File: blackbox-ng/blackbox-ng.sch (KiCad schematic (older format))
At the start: 19 parts

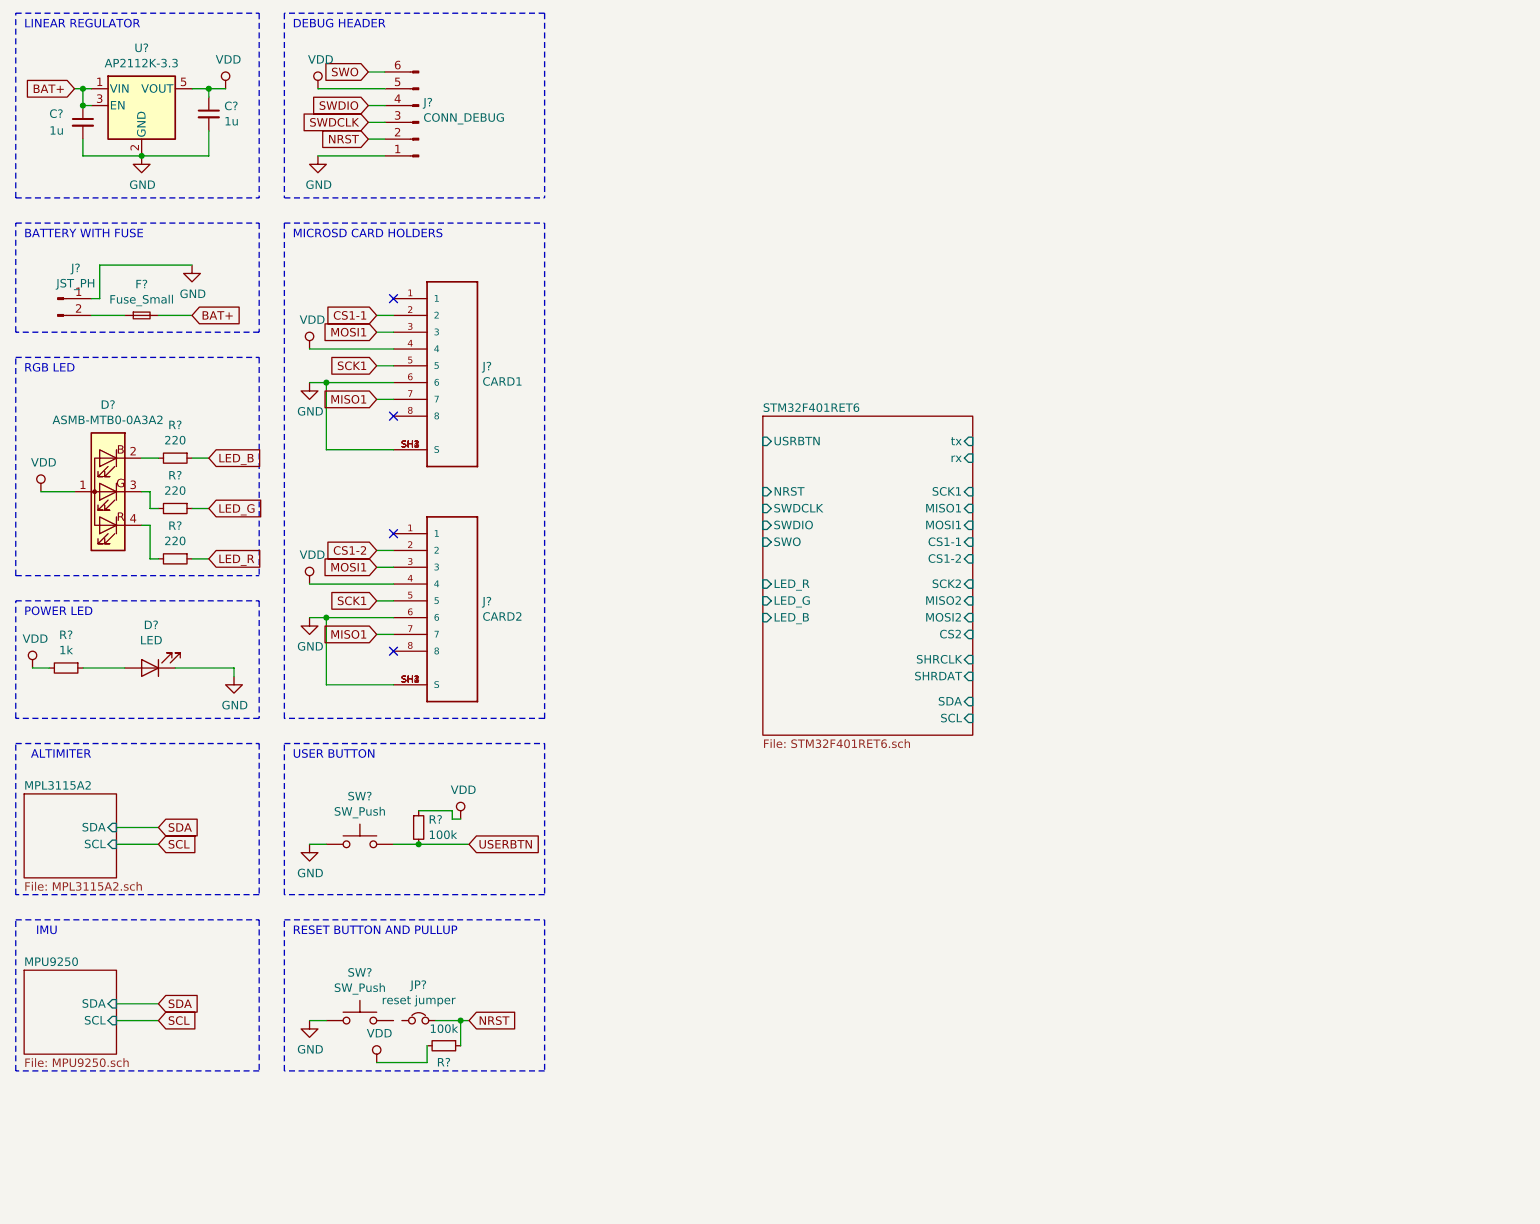
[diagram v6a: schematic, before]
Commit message: complete schematic
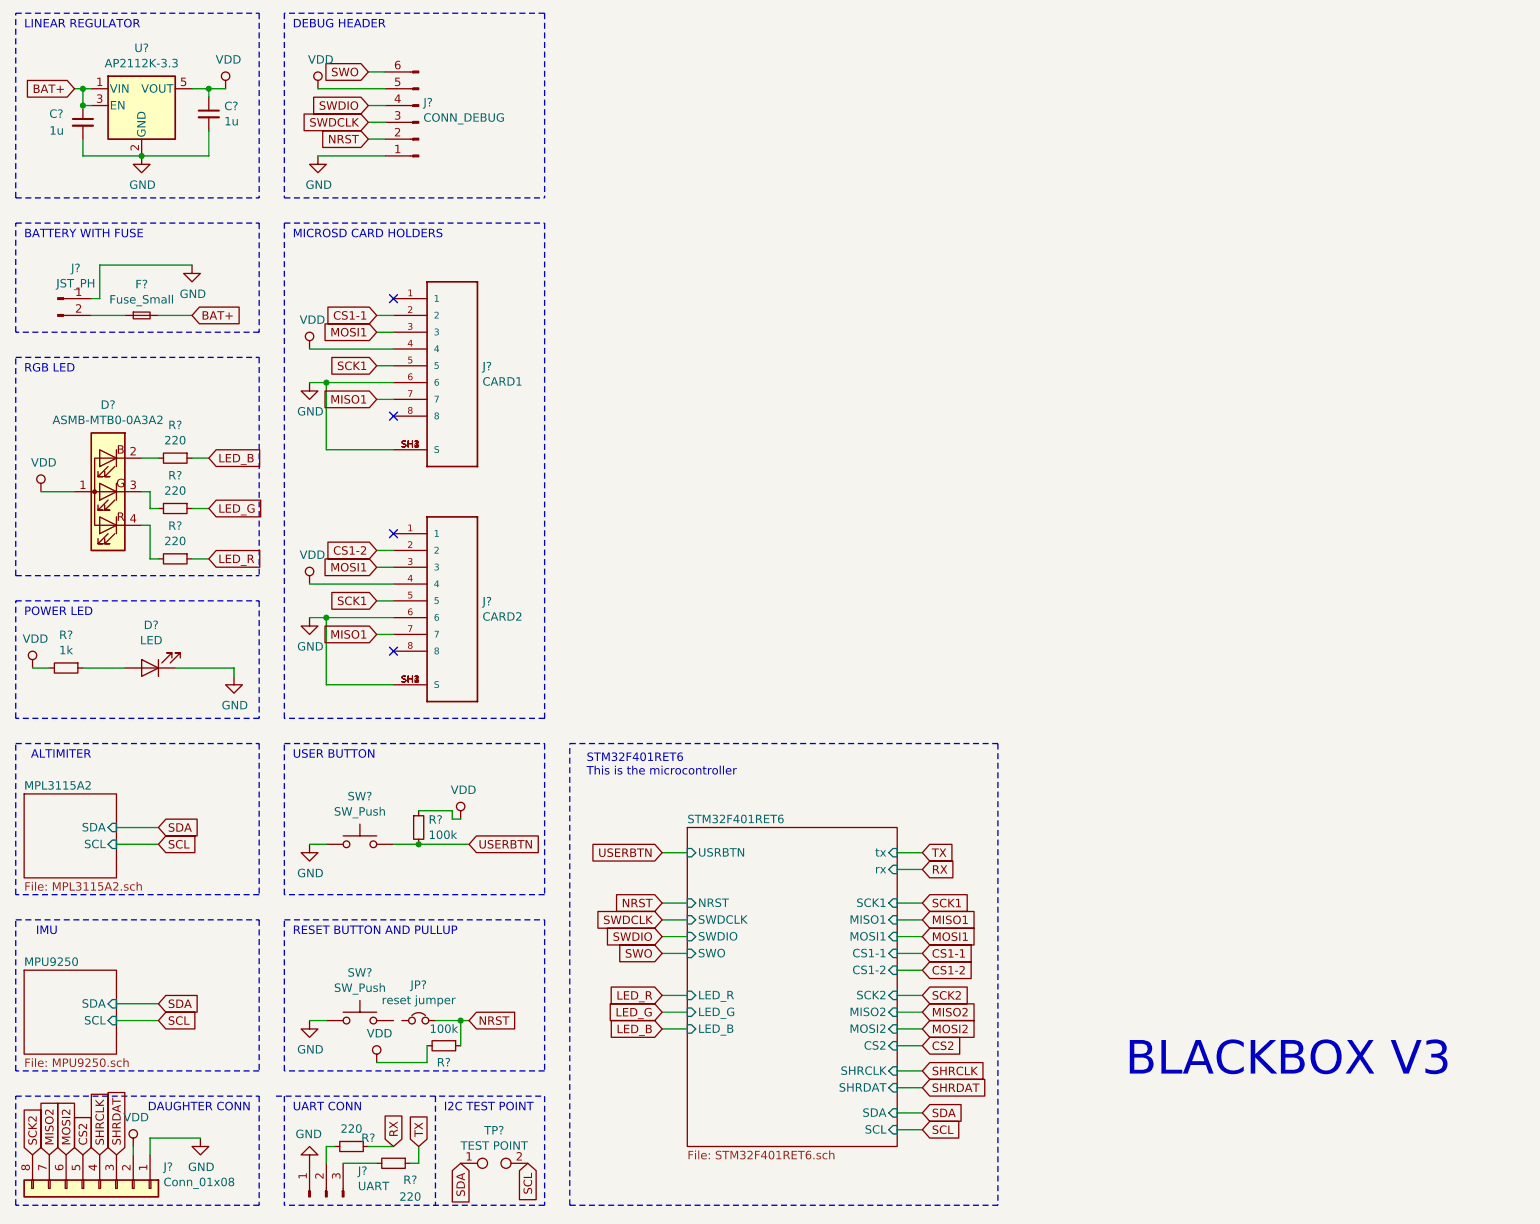
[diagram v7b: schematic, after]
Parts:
- added J?: Conn_01x08, symbol Connector_Generic:Conn_01x08
- added J?: UART, symbol Connector:Conn_01x03_Male
- added R? (x2): 220, symbol Device:R_Small
- added TP?: TEST POINT, symbol Connector:TestPoint_2Pole
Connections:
- net GND: now also J?.1 (Pin_1), J?.1 (Pin_1)
- net SCL: now also TP?.2
- net SDA: now also TP?.1
- net VDD: now also J?.2 (Pin_2)
- new net: J?.2 (Pin_2), R?.2
- new net: J?.3 (Pin_3), R?.2
- new net CS2: J?.5 (Pin_5)
- new net MISO2: J?.7 (Pin_7)
- new net MOSI2: J?.6 (Pin_6)
- new net RX: R?.1
- new net SCK2: J?.8 (Pin_8)
- new net SHRCLK: J?.4 (Pin_4)
- new net SHRDAT: J?.3 (Pin_3)
- new net TX: R?.1
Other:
- note added: "BLACKBOX V3"
- note added: "DAUGHTER CONN"
- note added: "I2C TEST POINT"
- note added: "STM32F401RET6\nThis is the microcontroller"
- note added: "UART CONN"

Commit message: assign footprints
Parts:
- C1, C2: renamed from C?; footprint (none) -> Capacitor_SMD:C_0603_1608Metric_Pad1.05x0.95mm_HandSolder
- D2: renamed from D?; footprint (none) -> LED_SMD:LED_0603_1608Metric_Castellated
- F1: renamed from F?; footprint (none) -> Fuse:Fuse_0603_1608Metric_Pad1.05x0.95mm_HandSolder
- J1: renamed from J?; footprint (none) -> Connector_PinHeader_2.54mm:PinHeader_1x06_P2.54mm_Vertical
- J2: renamed from J?; footprint (none) -> Connector_JST:JST_PH_B2B-PH-K_1x02_P2.00mm_Vertical
- J3, J4: renamed from J?; footprint MOLEX_500901-0801 -> blehhhh:MOLEX_500901-0801
- J5: renamed from J?; footprint (none) -> Connector_PinHeader_2.54mm:PinHeader_1x08_P2.54mm_Vertical
- J6: renamed from J?; footprint (none) -> Connector_PinHeader_2.54mm:PinHeader_1x03_P2.54mm_Vertical
- JP1: renamed from JP?; footprint (none) -> Jumper:SolderJumper-2_P1.3mm_Bridged2Bar_Pad1.0x1.5mm
- R1, R2, R3, R4, R5, R6, R7, R8: renamed from R?; footprint (none) -> Resistor_SMD:R_0603_1608Metric_Pad1.05x0.95mm_HandSolder
- SW1, SW2: renamed from SW?; footprint (none) -> Button_Switch_SMD:SW_SPST_B3S-1000
- TP1: renamed from TP?; footprint (none) -> TestPoint:TestPoint_2Pads_Pitch2.54mm_Drill0.8mm
- gave numbers to parts that had none: 2
